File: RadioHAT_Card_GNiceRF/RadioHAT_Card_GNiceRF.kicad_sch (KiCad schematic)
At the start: 10 parts, among them J2 Conn_Coaxial, J3 Conn_Coaxial, J4 Conn_Coaxial, J5 Conn_Coaxial, J6 Conn_Coaxial

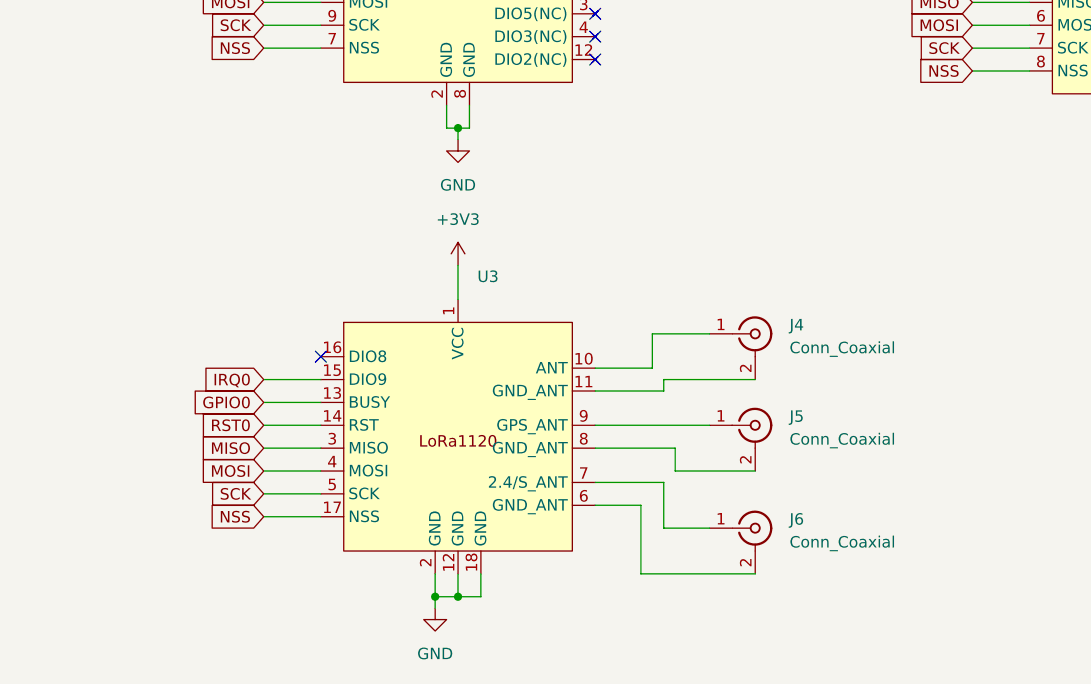
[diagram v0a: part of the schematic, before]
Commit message: Update G-NiceRF card to use LRxx21 instead of LR1120
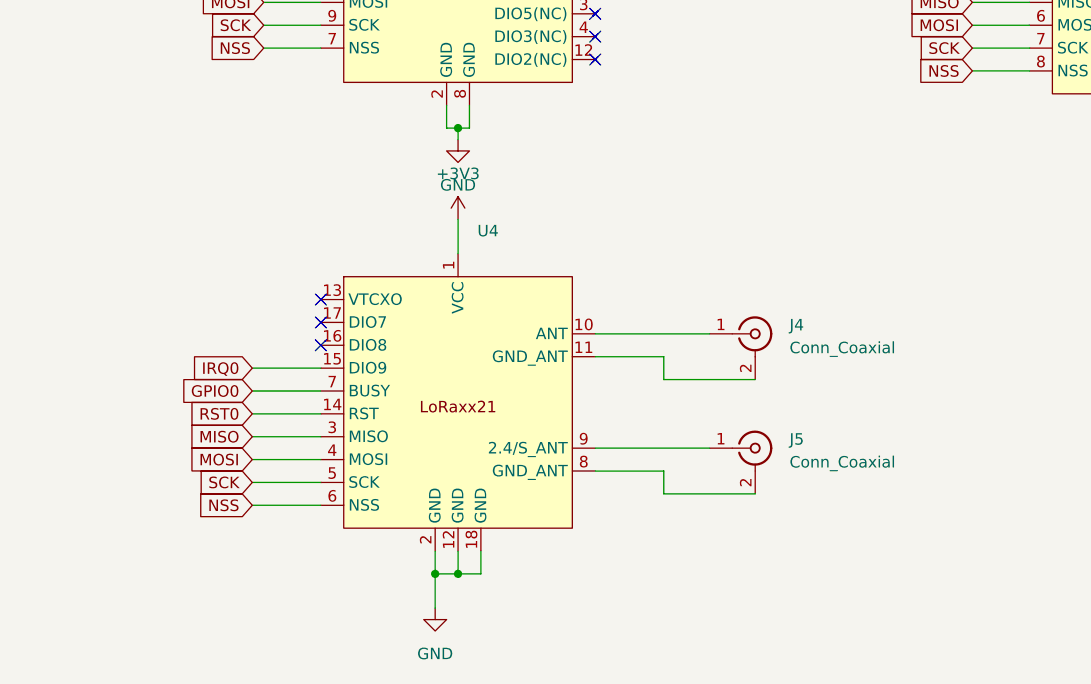
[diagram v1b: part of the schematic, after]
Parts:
- removed J6: Conn_Coaxial, Connector_Coaxial:U.FL_Molex_MCRF_73412-0110_Vertical, symbol Connector:Conn_Coaxial
- removed U3: ~, RadioHAT:LoRa1120, symbol RadioHAT:LoRa1120
- added U4: ~, RadioHAT:LoRaxx21, symbol RadioHAT:LoRaxx21
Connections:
- net +3V3: now also U4.1 (VCC)
- net GND: now also U4.12 (GND), U4.18 (GND), U4.2 (GND)
- net GPIO0: now also U4.7 (BUSY)
- net IRQ0: now also U4.15 (DIO9)
- net MISO: now also U4.3 (MISO)
- net MOSI: now also U4.4 (MOSI)
- net NSS: now also U4.6 (NSS)
- net RST0: now also U4.14 (RST)
- net SCK: now also U4.5 (SCK)
- net at J5.1 (In): now also U4.9 (2.4/S_ANT)
- net at J5.2 (Ext): now also U4.8 (GND_ANT)
- net at J4.1 (In): now also U4.10 (ANT)
- net at J4.2 (Ext): now also U4.11 (GND_ANT)
- no-connect marks 13 -> 15
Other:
- moved on the sheet: J5

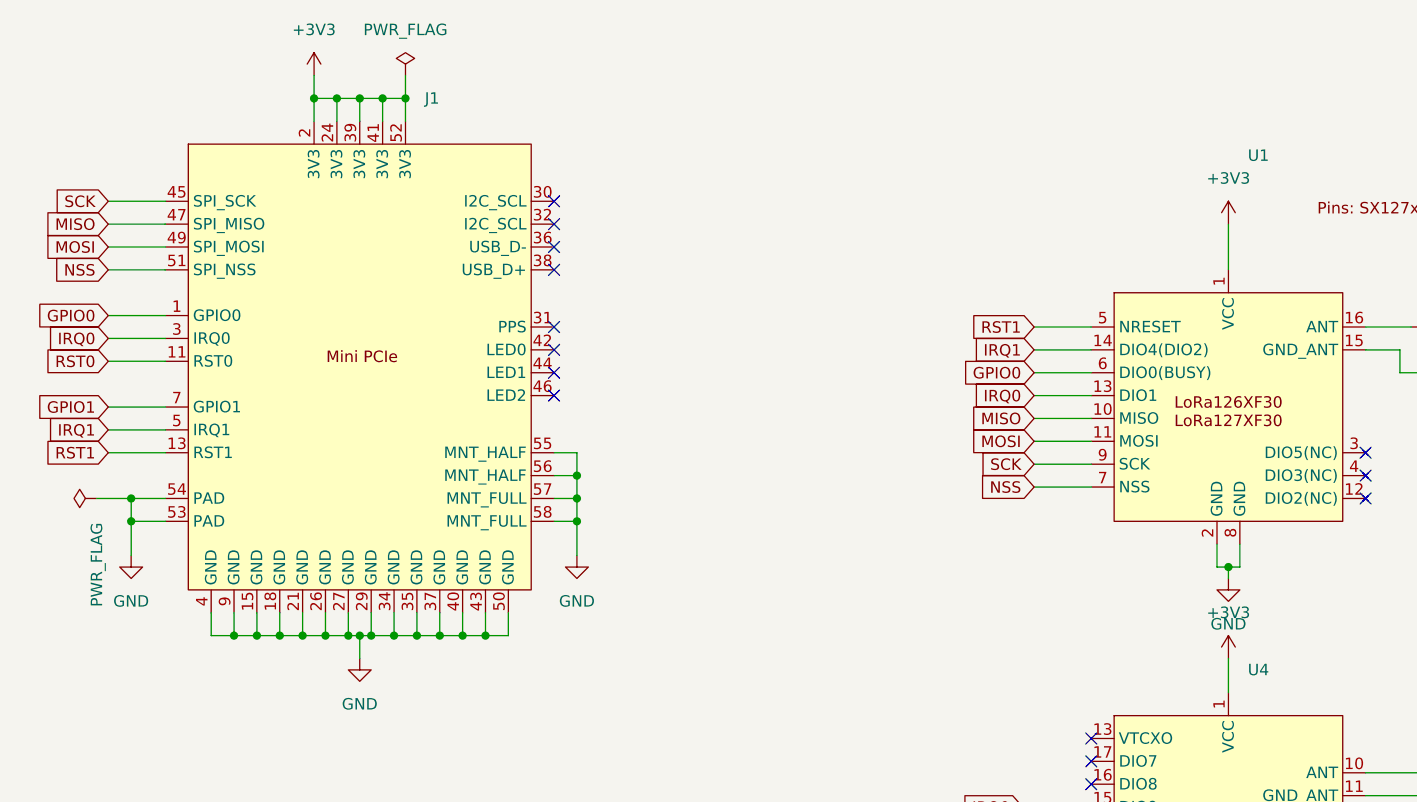
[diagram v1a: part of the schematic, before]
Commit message: Add 5V channel to GNiceRF card
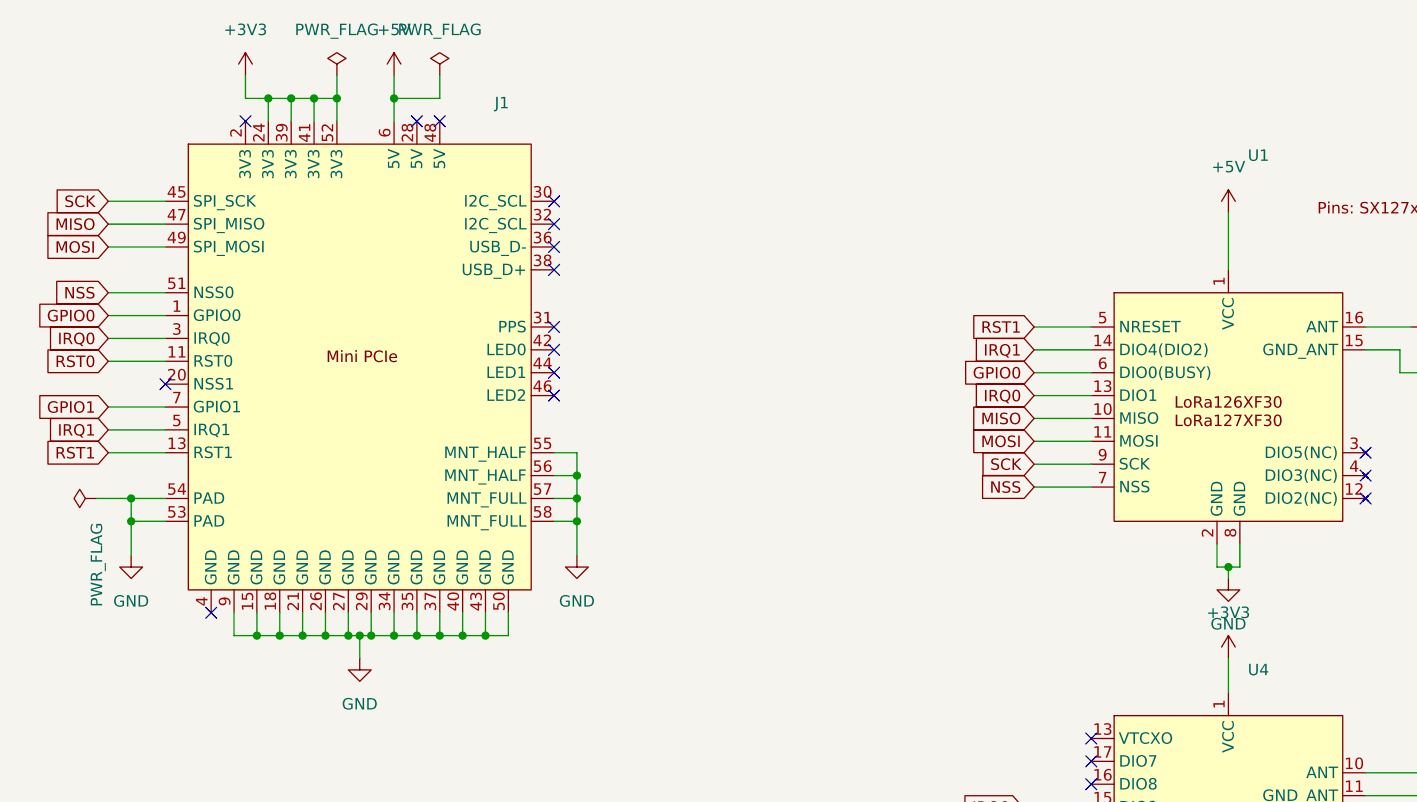
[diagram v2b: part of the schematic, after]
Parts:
- J1: Mouser (none) -> 571-1775838-2
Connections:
- net +3V3: no longer J1.2 (3V3), U1.1 (VCC)
- net GND: no longer J1.4 (GND)
- new net +5V: J1.6 (5V), U1.1 (VCC)
- no-connect marks 15 -> 20
